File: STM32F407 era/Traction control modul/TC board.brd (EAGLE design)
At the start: 160 x 100 mm, 10 parts, among them IC1 TL072D

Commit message: started work on traction control node
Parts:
- removed JP1, JP2: (no value), unicorn_v2:S2B-PH
- removed R4, R5: (no value), microbuilder:0603
- added C3, C4: 100n, microbuilder:_0603
- added D1: 1n5824, diode:F126Z12
- added H1, H2, H3, H4: MOUNT-HOLE3.0, holes:3,0
- added IC2: lm2575, linear:TO263-5
- added J1: (no value), unicorn_v2:AUTOCONNECTOR
- added L1: MSS1278-224KLD, SparkFun-Passives:CDRH125
- added U$1: CPU-BOARD, unicorn_v2:CPU-BOARD-JP1
- added U1: MAX13052ESA+, Maxim_By_element14_Batch_1:SOIC127P600X175-8N
- C1: value (none) -> 100u; device microbuilder:0603 -> rcl:E2,5-7
- C2: value (none) -> 220uf; device microbuilder:0603 -> rcl:E3,5-8
- IC1: value TL072D -> 74HC14D; device linear:SO08 -> 74xx-eu:SO14
- R1: value (none) -> 1k; device microbuilder:0603 -> microbuilder:_0603
- R2: value (none) -> 1k69; device microbuilder:0603 -> microbuilder:_0603
- R3: value (none) -> 1k8; device microbuilder:0603 -> microbuilder:_0603
- moved IC1 42.8 mm to (62.9, 59.7), turned to 90 degrees
- moved R3 39.0 mm to (50.2, 23.5), turned to 0 degrees
- moved C2 36.4 mm to (4.45, 68.6), turned to 180 degrees
- moved R2 27.7 mm to (6.35, 62.9), turned to 270 degrees
- moved C1 22.3 mm to (13.3, 68.6)
- moved R1 19.4 mm to (7.62, 62.9)
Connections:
- removed net N$7: IC1.7, JP2.1, R5.1
- removed net V+: IC1.8
- removed net V-: IC1.4
- new net 12V: C1.+, IC2.1, J1.M1
- new net 3.3V: C2.+, C3.1, C4.1, IC1.14, J1.E1, J1.E2, J1.E3, J1.E4, L1.2, R2.1, U$1.P$43, U$1.P$44, U1.3
- new net CANH: R3.2, U1.6
- new net CANL: R3.1, U1.7
- new net CAN_RX: U$1.P$55, U1.1
- new net CAN_TX: U$1.P$56, U1.4
- new net N$6: IC1.9, J1.B3
- new net RPM1: IC1.2, U$1.P$45
- new net RPM2: IC1.8, U$1.P$46
- new net RPM3: IC1.10, U$1.P$47
- new net RPM4: IC1.12, U$1.P$48
- new net TRAVEL1: J1.D2, U$1.P$1
- new net TRAVEL2: J1.D1, U$1.P$3
- new net TRAVEL3: J1.D3, U$1.P$5
- new net TRAVEL4: J1.D4, U$1.P$7
- net GND: now also C1.-, C2.-, C3.2, C4.2, D1.A, IC1.7, IC2.3, IC2.5, IC2.6, J1.A2, J1.A4, J1.B2, J1.B4, J1.C1, J1.C2, J1.C3, J1.C4, J1.L1, R1.1, U$1.P$21, U$1.P$22, U$1.P$41, U$1.P$42, U$1.P$62, U$1.P$69, U$1.P$70, U$1.P$78, U1.2, U1.8; no longer C2.1, IC1.6, R2.2, R5.2
- net N$1: now also IC2.4, R1.2, R2.2; no longer JP1.1, R4.2
- net N$2: now also D1.C, IC2.2, L1.1; no longer C1.1, R3.2, R4.1
- net N$3: now also IC1.11, J1.A1; no longer IC1.3, R3.1
- net N$4: now also IC1.13, J1.B1; no longer C1.2, IC1.1, IC1.5, R1.1
- net N$5: now also IC1.1, J1.A3; no longer IC1.2, R1.2, R2.1
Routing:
- net 3.3V: track 0.00 -> 189.3 mm, vias 0 -> 3
- net RPM2: track 0.00 -> 67.9 mm, vias 0 -> 1
- net RPM1: track 0.00 -> 63.5 mm, vias 0 -> 1
- net RPM3: track 0.00 -> 59.6 mm
- net RPM4: track 0.00 -> 58.3 mm
- net TRAVEL4: track 0.00 -> 30.8 mm
- net N$2: track 4.61 -> 30.5 mm
- net TRAVEL3: track 0.00 -> 25.8 mm
- net TRAVEL1: track 0.00 -> 22.7 mm
- net 12V: track 0.00 -> 20.2 mm
- net N$6: track 0.00 -> 18.4 mm
- net TRAVEL2: track 0.00 -> 17.7 mm
- net N$5: track 8.78 -> 25.3 mm
- net CAN_RX: track 0.00 -> 14.3 mm
- net GND: track 11.4 -> 0.00 mm
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- added copper zone on layer 1, net GND
- added copper zone on layer 16, net GND
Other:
- board size 160 x 100 mm -> 70.5 x 100 mm

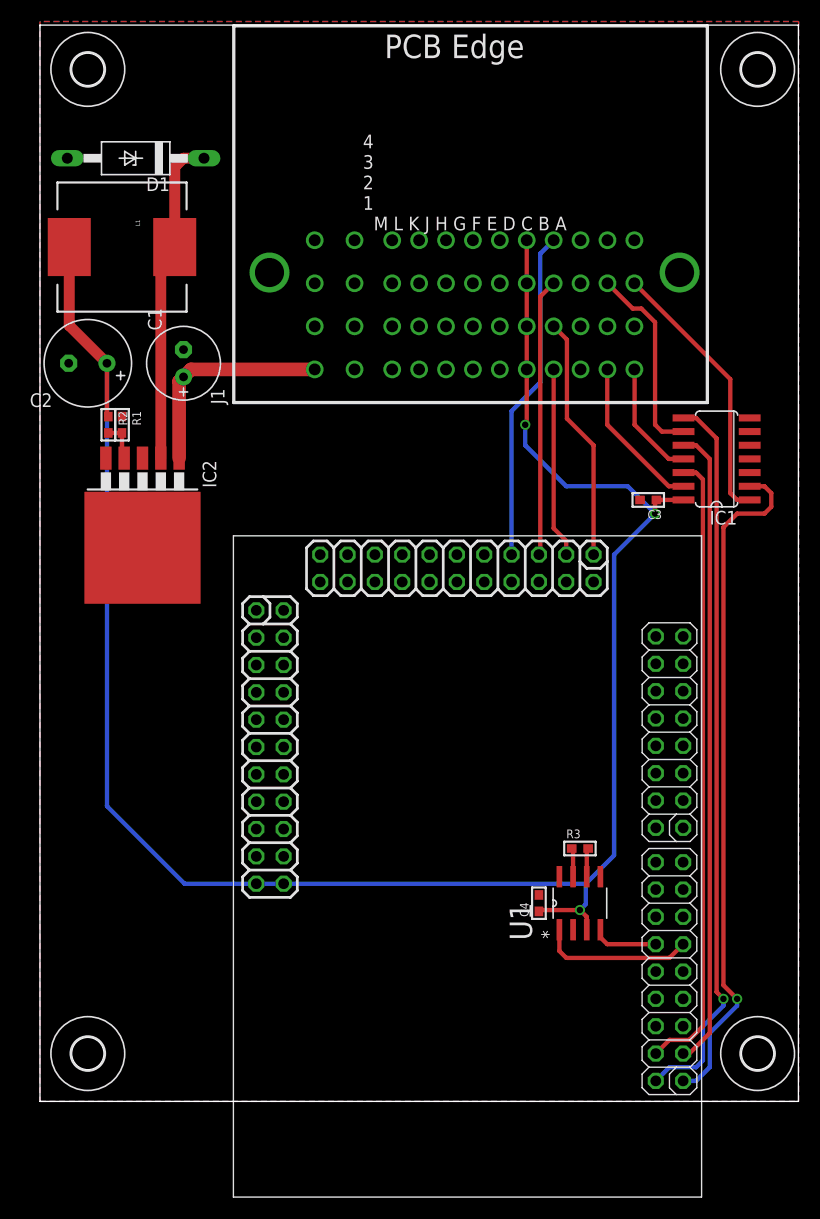
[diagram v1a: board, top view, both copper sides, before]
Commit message: small change to layout
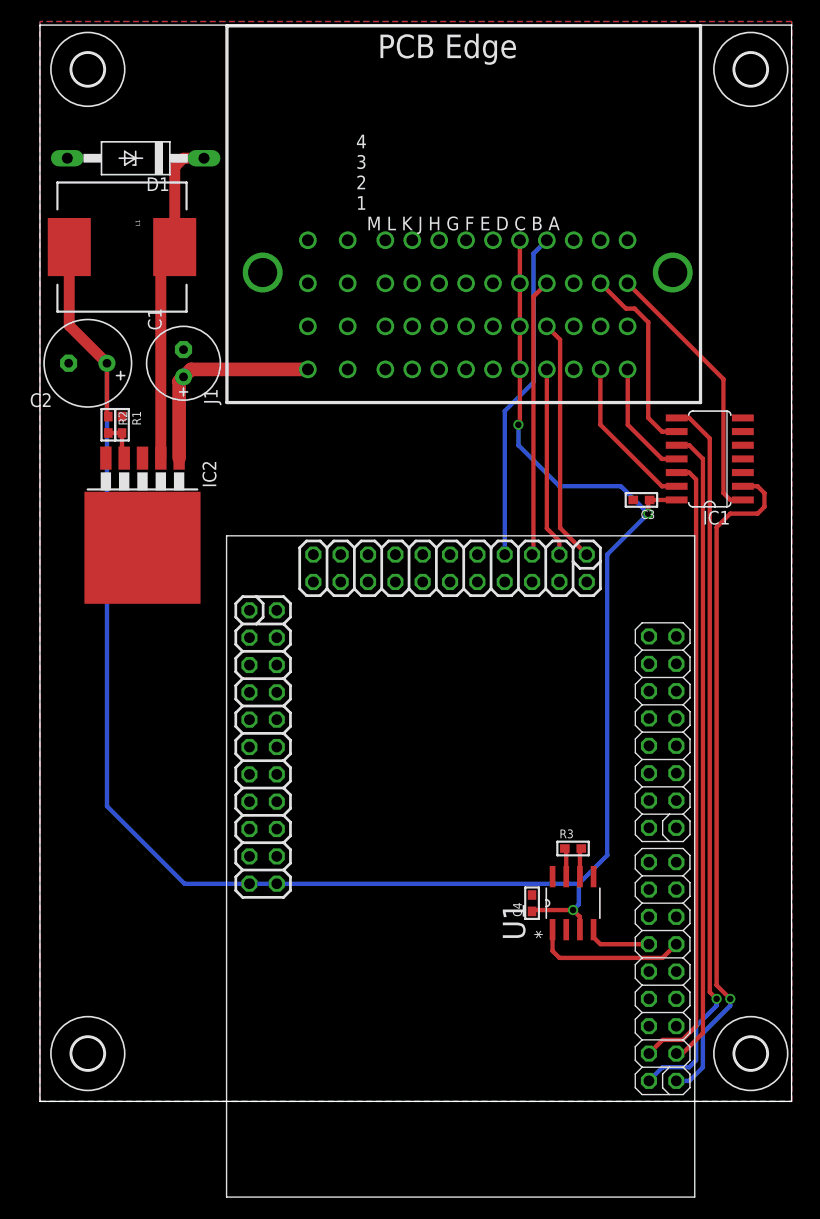
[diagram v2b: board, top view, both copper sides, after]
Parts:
- moved IC1 0.64 mm to (62.2, 59.7)
- moved J1 0.64 mm to (39.4, 74.9)
- moved C3 0.63 mm to (55.9, 55.9)
- moved C4 0.63 mm to (45.7, 18.4)
- moved R3 0.63 mm to (49.5, 23.5)
- moved U$1 0.63 mm to (38.1, 49.5)
- moved U1 0.63 mm to (49.5, 18.4)
- moved H1 0.63 mm to (66.0, 95.9)
- moved H4 0.63 mm to (66.0, 4.45)
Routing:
- net 12V: track 20.2 -> 19.6 mm
- net 3.3V: track 189.3 -> 188.6 mm
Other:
- board size 70.5 x 100 mm -> 69.8 x 100 mm

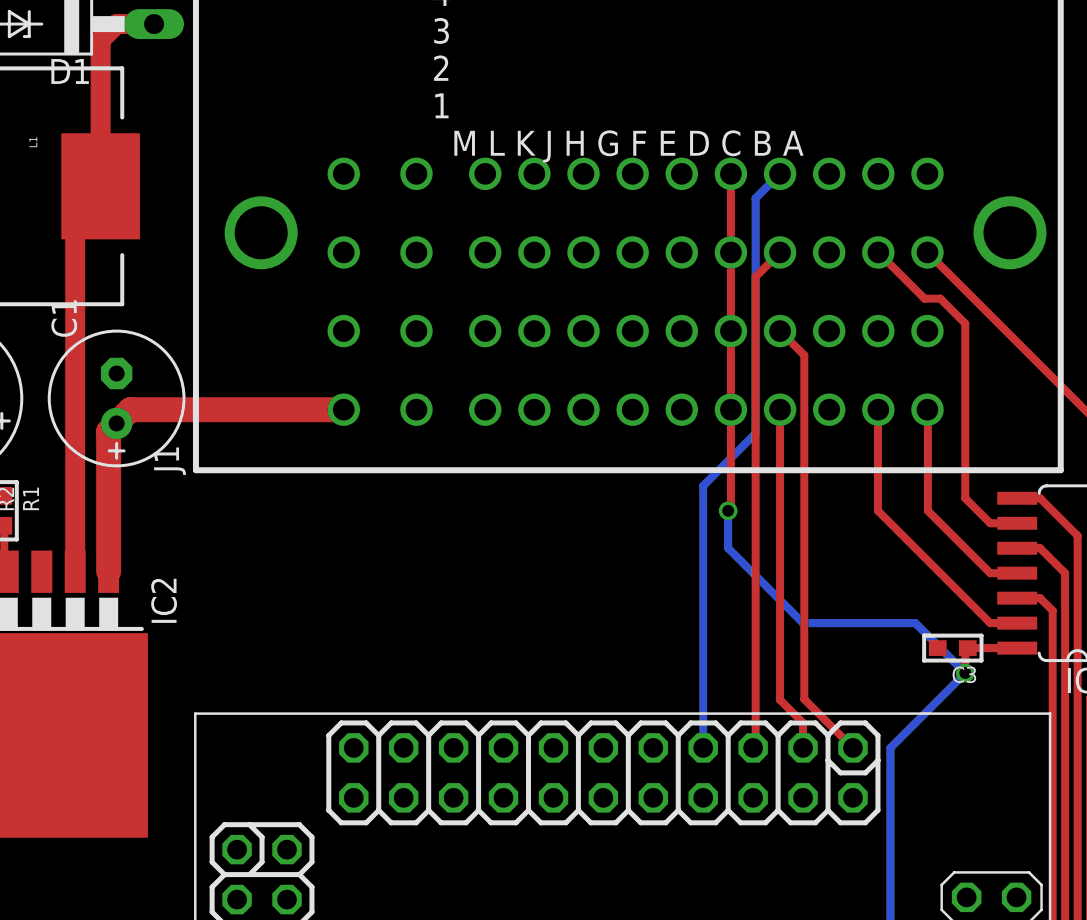
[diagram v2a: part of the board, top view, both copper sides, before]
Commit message: more work on TC, startet work on Aux sensor board
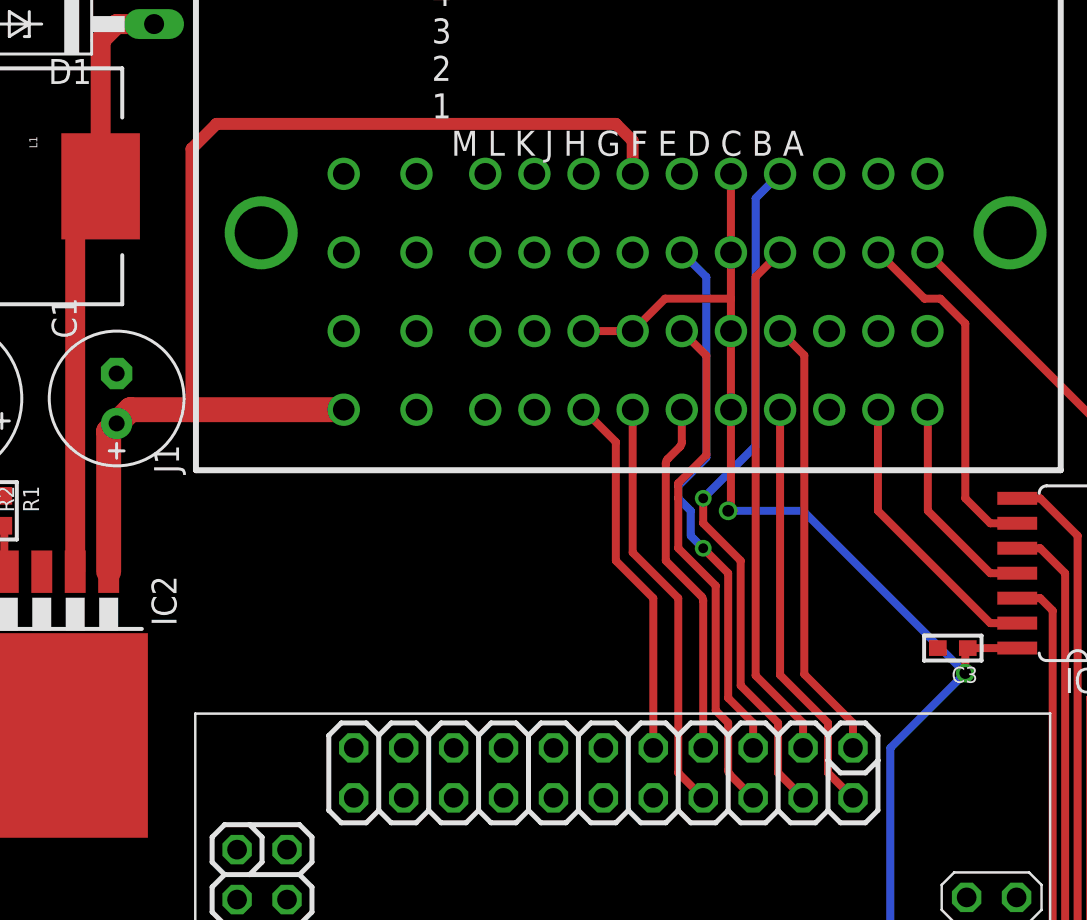
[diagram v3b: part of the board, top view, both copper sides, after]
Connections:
- new net BITE: J1.F3, U$1.P$5
- new net BRAKE-POT: J1.G1, U$1.P$8
- new net CLUTCH-POT: J1.H1, U$1.P$9
- new net GSENS: J1.F1, U$1.P$7
- new net YAW: J1.F2, U$1.P$6
- net 12V: now also J1.G4
- net 3.3V: now also J1.G2, J1.H2
- net GND: now also IC1.3, IC1.5, J1.F4, J1.G3, J1.H3
- net TRAVEL2: now also U$1.P$2; no longer U$1.P$3
- net TRAVEL3: now also U$1.P$3; no longer U$1.P$5
- net TRAVEL4: now also U$1.P$4; no longer U$1.P$7
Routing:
- net 12V: track 19.6 -> 57.8 mm
- net BITE: track 0.00 -> 27.9 mm, vias 0 -> 1
- net YAW: track 0.00 -> 26.4 mm
- net BRAKE-POT: track 0.00 -> 21.2 mm
- net CLUTCH-POT: track 0.00 -> 18.7 mm
- net GSENS: track 0.00 -> 18.3 mm
- net 3.3V: track 188.6 -> 195.7 mm
- net TRAVEL4: track 30.8 -> 35.5 mm, vias 0 -> 1
- net TRAVEL2: track 17.7 -> 21.3 mm
- net TRAVEL3: track 25.8 -> 26.7 mm
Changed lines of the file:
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@@
 <contactref element="J1" pad="C4"/>
 <contactref element="J1" pad="C3"/>
+<contactref element="J1" pad="F4"/>
+<contactref element="J1" pad="G3"/>
+<contactref element="J1" pad="H3"/>
+<contactref element="IC1" pad="3"/>
+<contactref element="IC1" pad="5"/>
 </signal>
 <signal name="3.3V">
@@
 <contactref element="J1" pad="E3"/>
 <wire x1="44.59" y1="80.01" x2="44.59" y2="76.01" width="0.4064" layer="1"/>
-<wire x1="44.59" y1="76.01" x2="44.59" y2="72.01" width="0.4064" layer="1"/>
+<wire x1="44.59" y1="76.01" x2="44.59" y2="73.66" width="0.4064" layer="1"/>
+<wire x1="44.59" y1="73.66" x2="44.59" y2="72.01" width="0.4064" layer="1"/>
 <wire x1="44.59" y1="72.01" x2="44.59" y2="68.01" width="0.4064" layer="1"/>
 <wire x1="44.59" y1="68.01" x2="44.59" y2="63.005" width="0.4064" layer="1"/>
 <wire x1="44.59" y1="63.005" x2="44.45" y2="62.865" width="0.4064" layer="1"/>
 <via x="44.45" y="62.865" extent="1-16" drill="0.6" shape="octagon"/>
-<wire x1="44.45" y1="62.865" x2="44.45" y2="60.96" width="0.4064" layer="16"/>
-<wire x1="44.45" y1="60.96" x2="48.26" y2="57.15" width="0.4064" layer="16"/>
-<wire x1="48.26" y1="57.15" x2="53.975" y2="57.15" width="0.4064" layer="16"/>
-<wire x1="53.975" y1="57.15" x2="56.515" y2="54.61" width="0.4064" layer="16"/>
+<wire x1="44.45" y1="62.865" x2="48.26" y2="62.865" width="0.4064" layer="16"/>
+<wire x1="48.26" y1="62.865" x2="56.515" y2="54.61" width="0.4064" layer="16"/>
+<contactref element="J1" pad="G2"/>
+<contactref element="J1" pad="H2"/>
+<wire x1="37.09" y1="72.01" x2="39.59" y2="72.01" width="0.4064" layer="1"/>
+<wire x1="39.59" y1="72.01" x2="41.24" y2="73.66" width="0.4064" layer="1"/>
+<wire x1="41.24" y1="73.66" x2="44.59" y2="73.66" width="0.4064" layer="1"/>
 </signal>
 <signal name="12V">
@@
 <contactref element="J1" pad="M1"/>
 <contactref element="C1" pad="+"/>
-<wire x1="24.89" y1="68.01" x2="14.035" y2="68.01" width="1.27" layer="1"/>
+<wire x1="24.89" y1="68.01" x2="17.145" y2="68.01" width="1.27" layer="1"/>
+<wire x1="17.145" y1="68.01" x2="14.035" y2="68.01" width="1.27" layer="1"/>
 <wire x1="14.035" y1="68.01" x2="13.335" y2="67.31" width="1.27" layer="1"/>
 <wire x1="13.335" y1="67.31" x2="12.9286" y2="66.9036" width="1.27" layer="1"/>
 <wire x1="12.9286" y1="66.9036" x2="12.9286" y2="59.7662" width="1.27" layer="1"/>
+<contactref element="J1" pad="G4"/>
+<wire x1="39.59" y1="80.01" x2="39.59" y2="81.695" width="0.6096" layer="1"/>
+<wire x1="39.59" y1="81.695" x2="38.735" y2="82.55" width="0.6096" layer="1"/>
+<wire x1="38.735" y1="82.55" x2="18.415" y2="82.55" width="0.6096" layer="1"/>
+<wire x1="18.415" y1="82.55" x2="17.145" y2="81.28" width="0.6096" layer="1"/>
+<wire x1="17.145" y1="81.28" x2="17.145" y2="68.01" width="0.6096" layer="1"/>
 </signal>
 <signal name="N$1">
@@
 <contactref element="J1" pad="D2"/>
 <wire x1="47.09" y1="72.01" x2="48.3235" y2="70.7765" width="0.4064" layer="1"/>
-<wire x1="48.3235" y1="70.7765" x2="48.3235" y2="53.2765" width="0.4064" layer="1"/>
-<wire x1="48.3235" y1="53.2765" x2="50.8" y2="50.8" width="0.4064" layer="1"/>
+<wire x1="48.3235" y1="70.7765" x2="48.3235" y2="54.5465" width="0.4064" layer="1"/>
+<wire x1="48.3235" y1="54.5465" x2="50.8" y2="52.07" width="0.4064" layer="1"/>
+<wire x1="50.8" y1="52.07" x2="50.8" y2="50.8" width="0.4064" layer="1"/>
 </signal>
 <signal name="TRAVEL2">
-<contactref element="U$1" pad="P$3"/>
 <contactref element="J1" pad="D1"/>
-<wire x1="48.26" y1="50.8" x2="48.26" y2="52.07" width="0.4064" layer="1"/>
-<wire x1="48.26" y1="52.07" x2="47.09" y2="53.24" width="0.4064" layer="1"/>
-<wire x1="47.09" y1="53.24" x2="47.09" y2="68.01" width="0.4064" layer="1"/>
+<contactref element="U$1" pad="P$2"/>
+<wire x1="47.09" y1="54.51" x2="47.09" y2="68.01" width="0.4064" layer="1"/>
+<wire x1="50.8" y1="48.26" x2="49.53" y2="49.53" width="0.4064" layer="1"/>
+<wire x1="49.53" y1="49.53" x2="49.53" y2="52.07" width="0.4064" layer="1"/>
+<wire x1="49.53" y1="52.07" x2="47.09" y2="54.51" width="0.4064" layer="1"/>
 </signal>
 <signal name="TRAVEL3">
-<contactref element="U$1" pad="P$5"/>
 <contactref element="J1" pad="D3"/>
 <wire x1="47.09" y1="76.01" x2="45.847" y2="74.767" width="0.4064" layer="1"/>
-<wire x1="45.847" y1="74.767" x2="45.847" y2="50.927" width="0.4064" layer="1"/>
-<wire x1="45.847" y1="50.927" x2="45.72" y2="50.8" width="0.4064" layer="1"/>
+<wire x1="45.847" y1="74.767" x2="45.847" y2="54.483" width="0.4064" layer="1"/>
+<contactref element="U$1" pad="P$3"/>
+<wire x1="45.847" y1="54.483" x2="48.26" y2="52.07" width="0.4064" layer="1"/>
+<wire x1="48.26" y1="52.07" x2="48.26" y2="50.8" width="0.4064" layer="1"/>
 </signal>
 <signal name="TRAVEL4">
-<contactref element="U$1" pad="P$7"/>
 <contactref element="J1" pad="D4"/>
 <wire x1="47.09" y1="80.01" x2="45.847" y2="78.767" width="0.4064" layer="16"/>
-<wire x1="45.847" y1="78.767" x2="45.847" y2="66.802" width="0.4064" layer="16"/>
-<wire x1="45.847" y1="66.802" x2="43.18" y2="64.135" width="0.4064" layer="16"/>
-<wire x1="43.18" y1="64.135" x2="43.18" y2="50.8" width="0.4064" layer="16"/>
+<wire x1="45.847" y1="78.767" x2="45.847" y2="66.167" width="0.4064" layer="16"/>
+<wire x1="45.847" y1="66.167" x2="43.18" y2="63.5" width="0.4064" layer="16"/>
+<contactref element="U$1" pad="P$4"/>
+<via x="43.18" y="63.5" extent="1-16" drill="0.5" shape="octagon"/>
+<wire x1="43.18" y1="63.5" x2="43.18" y2="62.23" width="0.4064" layer="1"/>
+<wire x1="43.18" y1="62.23" x2="45.085" y2="60.325" width="0.4064" layer="1"/>
+<wire x1="45.085" y1="60.325" x2="45.085" y2="53.975" width="0.4064" layer="1"/>
+<wire x1="45.085" y1="53.975" x2="46.99" y2="52.07" width="0.4064" layer="1"/>
+<wire x1="46.99" y1="52.07" x2="46.99" y2="49.53" width="0.4064" layer="1"/>
+<wire x1="46.99" y1="49.53" x2="48.26" y2="48.26" width="0.4064" layer="1"/>
+</signal>
+<signal name="GSENS">
+<contactref element="J1" pad="F1"/>
+<contactref element="U$1" pad="P$7"/>
+<wire x1="43.18" y1="50.8" x2="43.18" y2="58.2884875" width="0.4064" layer="1"/>
+<wire x1="43.18" y1="58.2884875" x2="43.08700625" y2="58.51299375" width="0.4064" layer="1" curve="45"/>
+<wire x1="43.08700625" y1="58.51299375" x2="41.275" y2="60.325" width="0.4064" layer="1"/>
+<wire x1="41.275" y1="60.325" x2="41.275" y2="65.2734875" width="0.4064" layer="1"/>
+<wire x1="41.275" y1="65.2734875" x2="41.36799375" y2="65.49799375" width="0.4064" layer="1" curve="-45"/>
+<wire x1="41.36799375" y1="65.49799375" x2="41.99700625" y2="66.12700625" width="0.4064" layer="1"/>
+<wire x1="41.99700625" y1="66.12700625" x2="42.09" y2="66.3515125" width="0.4064" layer="1" curve="45"/>
+<wire x1="42.09" y1="66.3515125" x2="42.09" y2="68.01" width="0.4064" layer="1"/>
+</signal>
+<signal name="YAW">
+<contactref element="J1" pad="F2"/>
+<contactref element="U$1" pad="P$6"/>
+<wire x1="42.09" y1="72.01" x2="43.33875" y2="70.76125" width="0.4064" layer="1"/>
+<wire x1="43.33875" y1="70.76125" x2="43.33875" y2="65.6952625" width="0.4064" layer="1"/>
+<wire x1="44.45" y1="52.07" x2="44.45" y2="49.6615125" width="0.4064" layer="1"/>
+<wire x1="44.45" y1="49.6615125" x2="44.54299375" y2="49.43700625" width="0.4064" layer="1" curve="45"/>
+<wire x1="44.54299375" y1="49.43700625" x2="45.72" y2="48.26" width="0.4064" layer="1"/>
+<wire x1="44.45" y1="52.07" x2="43.815" y2="52.705" width="0.4064" layer="1"/>
+<wire x1="43.33875" y1="65.6952625" x2="41.91" y2="64.2665125" width="0.4064" layer="1"/>
+<wire x1="41.91" y1="64.2665125" x2="41.91" y2="60.96" width="0.4064" layer="1"/>
+<wire x1="41.91" y1="60.96" x2="43.815" y2="59.055" width="0.4064" layer="1"/>
+<wire x1="43.815" y1="59.055" x2="43.815" y2="52.705" width="0.4064" layer="1"/>
+</signal>
+<signal name="BITE">
+<contactref element="J1" pad="F3"/>
+<contactref element="U$1" pad="P$5"/>
+<wire x1="45.72" y1="50.8" x2="45.72" y2="52.07" width="0.4064" layer="1"/>
+<wire x1="45.72" y1="52.07" x2="44.45" y2="53.34" width="0.4064" layer="1"/>
+<wire x1="44.45" y1="53.34" x2="44.45" y2="59.69" width="0.4064" layer="1"/>
+<wire x1="44.45" y1="59.69" x2="43.18" y2="60.96" width="0.4064" layer="1"/>
+<via x="43.18" y="60.96" extent="1-16" drill="0.5" shape="octagon"/>
+<wire x1="43.18" y1="60.96" x2="42.545" y2="61.595" width="0.4064" layer="16"/>
+<wire x1="42.545" y1="61.595" x2="42.545" y2="62.865" width="0.4064" layer="16"/>
+<wire x1="42.545" y1="62.865" x2="41.91" y2="63.5" width="0.4064" layer="16"/>
+<wire x1="41.91" y1="63.5" x2="41.91" y2="64.135" width="0.4064" layer="16"/>
+<wire x1="41.91" y1="64.135" x2="43.33875" y2="65.56375" width="0.4064" layer="16"/>
+<wire x1="43.33875" y1="65.56375" x2="43.33875" y2="74.76125" width="0.4064" layer="16"/>
+<wire x1="43.33875" y1="74.76125" x2="42.09" y2="76.01" width="0.4064" layer="16"/>
+</signal>
+<signal name="BRAKE-POT">
+<contactref element="U$1" pad="P$8"/>
+<contactref element="J1" pad="G1"/>
+<wire x1="43.18" y1="48.26" x2="41.91" y2="49.53" width="0.4064" layer="1"/>
+<wire x1="41.91" y1="49.53" x2="41.91" y2="58.42" width="0.4064" layer="1"/>
+<wire x1="41.91" y1="58.42" x2="39.59" y2="60.74" width="0.4064" layer="1"/>
+<wire x1="39.59" y1="60.74" x2="39.59" y2="68.01" width="0.4064" layer="1"/>
+</signal>
+<signal name="CLUTCH-POT">
+<contactref element="U$1" pad="P$9"/>
+<contactref element="J1" pad="H1"/>
+<wire x1="37.09" y1="68.01" x2="38.735" y2="66.365" width="0.4064" layer="1"/>
+<wire x1="38.735" y1="66.365" x2="38.735" y2="60.325" width="0.4064" layer="1"/>
+<wire x1="38.735" y1="60.325" x2="40.64" y2="58.42" width="0.4064" layer="1"/>
+<wire x1="40.64" y1="58.42" x2="40.64" y2="50.8" width="0.4064" layer="1"/>
 </signal>
 </signals>
